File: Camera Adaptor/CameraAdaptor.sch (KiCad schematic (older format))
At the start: 6 parts

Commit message: Did the basic layout, avaiting via size, track width specifications.
Signed-off-by: Kolijn Wolfaardt <kolijn.wolfaardt@gmail.com>
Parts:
- C1: renamed from C?; footprint (none) -> Capacitors_SMD:C_1206_HandSoldering
- P1: renamed from P?; footprint (none) -> Pin_Headers:Pin_Header_Straight_2x12
- P2: renamed from P?; footprint (none) -> Pin_Headers:Pin_Header_Straight_2x09
- R1, R2: renamed from 4k7; value R -> 4.7k; footprint (none) -> Resistors_SMD:R_1206_HandSoldering
- U1: renamed from U?; footprint (none) -> oscillator:oscillator
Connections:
- no-connect marks 3 -> 4
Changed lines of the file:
@@
 $EndDescr
 $Comp
-L CONN_02X12 P?
+L CONN_02X12 P1
 U 1 1 5583E006
 P 3350 3250
-F 0 "P?" H 3350 3900 50  0000 C CNN
+F 0 "P1" H 3350 3900 50  0000 C CNN
 F 1 "CONN_02X12" V 3350 3250 50  0000 C CNN
-F 2 "" H 3350 2050 60  0000 C CNN
+F 2 "Pin_Headers:Pin_Header_Straight_2x12" H 3350 2050 60  0001 C CNN
 F 3 "" H 3350 2050 60  0000 C CNN
 	1    3350 3250
@@
 $EndComp
 $Comp
-L CONN_02X09 P?
+L CONN_02X09 P2
 U 1 1 5583E070
 P 5850 3200
-F 0 "P?" H 5850 3700 50  0000 C CNN
+F 0 "P2" H 5850 3700 50  0000 C CNN
 F 1 "CONN_02X09" V 5850 3200 50  0000 C CNN
-F 2 "" H 5850 2000 60  0000 C CNN
+F 2 "Pin_Headers:Pin_Header_Straight_2x09" H 5850 2000 60  0001 C CNN
 F 3 "" H 5850 2000 60  0000 C CNN
 	1    5850 3200
@@
 D0
 $Comp
-L R 4k7
+L R R1
 U 1 1 55C45043
 P 4550 1850
-F 0 "4k7" V 4630 1850 50  0000 C CNN
-F 1 "R" V 4550 1850 50  0000 C CNN
-F 2 "" V 4480 1850 30  0000 C CNN
+F 0 "R1" V 4630 1850 50  0000 C CNN
+F 1 "4.7k" V 4550 1850 50  0000 C CNN
+F 2 "Resistors_SMD:R_1206_HandSoldering" V 4480 1850 30  0001 C CNN
 F 3 "" H 4550 1850 30  0000 C CNN
 	1    4550 1850
@@
 $EndComp
 $Comp
-L R 4k7
+L R R2
 U 1 1 55C450E0
 P 4800 1850
-F 0 "4k7" V 4880 1850 50  0000 C CNN
-F 1 "R" V 4800 1850 50  0000 C CNN
-F 2 "" V 4730 1850 30  0000 C CNN
+F 0 "R2" V 4880 1850 50  0000 C CNN
+F 1 "4.7k" V 4800 1850 50  0000 C CNN
+F 2 "Resistors_SMD:R_1206_HandSoldering" V 4730 1850 30  0001 C CNN
 F 3 "" H 4800 1850 30  0000 C CNN
 	1    4800 1850
@@
 $EndComp
 $Comp
-L GND #PWR?
+L GND #PWR01
 U 1 1 55C45174
 P 4200 2700
-F 0 "#PWR?" H 4200 2450 50  0001 C CNN
+F 0 "#PWR01" H 4200 2450 50  0001 C CNN
 F 1 "GND" H 4200 2550 50  0000 C CNN
 F 2 "" H 4200 2700 60  0000 C CNN
@@
 $EndComp
 $Comp
-L +3.3V #PWR?
+L +3.3V #PWR02
 U 1 1 55C451A0
 P 2500 2700
-F 0 "#PWR?" H 2500 2550 50  0001 C CNN
+F 0 "#PWR02" H 2500 2550 50  0001 C CNN
 F 1 "+3.3V" H 2500 2840 50  0000 C CNN
 F 2 "" H 2500 2700 60  0000 C CNN
@@
 $EndComp
 $Comp
-L +3.3V #PWR?
+L +3.3V #PWR03
 U 1 1 55C45250
 P 4700 1600
-F 0 "#PWR?" H 4700 1450 50  0001 C CNN
+F 0 "#PWR03" H 4700 1450 50  0001 C CNN
 F 1 "+3.3V" H 4700 1740 50  0000 C CNN
 F 2 "" H 4700 1600 60  0000 C CNN
@@
 NoConn ~ 3600 3800
 $Comp
-L GND #PWR?
+L GND #PWR04
 U 1 1 55C45C7F
 P 4200 3450
-F 0 "#PWR?" H 4200 3200 50  0001 C CNN
+F 0 "#PWR04" H 4200 3200 50  0001 C CNN
 F 1 "GND" H 4200 3300 50  0000 C CNN
 F 2 "" H 4200 3450 60  0000 C CNN
@@
 	2500 3400 3100 3400
 $Comp
-L C C?
+L C C1
 U 1 1 55C45D20
 P 3100 1850
-F 0 "C?" H 3125 1950 50  0000 L CNN
+F 0 "C1" H 3125 1950 50  0000 L CNN
 F 1 "1uF" H 3125 1750 50  0000 L CNN
-F 2 "" H 3138 1700 30  0000 C CNN
+F 2 "Capacitors_SMD:C_1206_HandSoldering" H 3138 1700 30  0001 C CNN
 F 3 "" H 3100 1850 60  0000 C CNN
 	1    3100 1850
@@
 $EndComp
 $Comp
-L +3.3V #PWR?
+L +3.3V #PWR05
 U 1 1 55C45D93
 P 3100 1650
-F 0 "#PWR?" H 3100 1500 50  0001 C CNN
+F 0 "#PWR05" H 3100 1500 50  0001 C CNN
 F 1 "+3.3V" H 3100 1790 50  0000 C CNN
 F 2 "" H 3100 1650 60  0000 C CNN
@@
 $EndComp
 $Comp
-L GND #PWR?
+L GND #PWR06
 U 1 1 55C45DA8
 P 3100 2050
-F 0 "#PWR?" H 3100 1800 50  0001 C CNN
+F 0 "#PWR06" H 3100 1800 50  0001 C CNN
 F 1 "GND" H 3100 1900 50  0000 C CNN
 F 2 "" H 3100 2050 60  0000 C CNN
@@
 	3100 1700 3100 1650
 $Comp
-L Oscillator U?
+L Oscillator U1
 U 1 1 55C47029
 P 4500 4650
-F 0 "U?" H 4500 4400 60  0000 C CNN
+F 0 "U1" H 4500 4400 60  0000 C CNN
 F 1 "Oscillator" H 4500 4900 60  0000 C CNN
-F 2 "" H 4500 4650 60  0000 C CNN
+F 2 "oscillator:oscillator" H 4500 4650 60  0001 C CNN
 F 3 "" H 4500 4650 60  0000 C CNN
 	1    4500 4650
@@
 $EndComp
 $Comp
-L +3.3V #PWR?
+L +3.3V #PWR07
 U 1 1 55C47102
 P 5100 4450
-F 0 "#PWR?" H 5100 4300 50  0001 C CNN
+F 0 "#PWR07" H 5100 4300 50  0001 C CNN
 F 1 "+3.3V" H 5100 4590 50  0000 C CNN
 F 2 "" H 5100 4450 60  0000 C CNN
@@
 	5100 4550 5100 4450
 $Comp
-L GND #PWR?
+L GND #PWR08
 U 1 1 55C471E4
 P 3900 4850
-F 0 "#PWR?" H 3900 4600 50  0001 C CNN
+F 0 "#PWR08" H 3900 4600 50  0001 C CNN
 F 1 "GND" H 3900 4700 50  0000 C CNN
 F 2 "" H 3900 4850 60  0000 C CNN
@@
 PCLK
 $Comp
-L +3.3V #PWR?
+L +3.3V #PWR09
 U 1 1 55C476CA
 P 3900 4450
-F 0 "#PWR?" H 3900 4300 50  0001 C CNN
+F 0 "#PWR09" H 3900 4300 50  0001 C CNN
 F 1 "+3.3V" H 3900 4590 50  0000 C CNN
 F 2 "" H 3900 4450 60  0000 C CNN
@@
 Wire Wire Line
 	3900 4550 4000 4550
+NoConn ~ 3100 3600
 $EndSCHEMATC

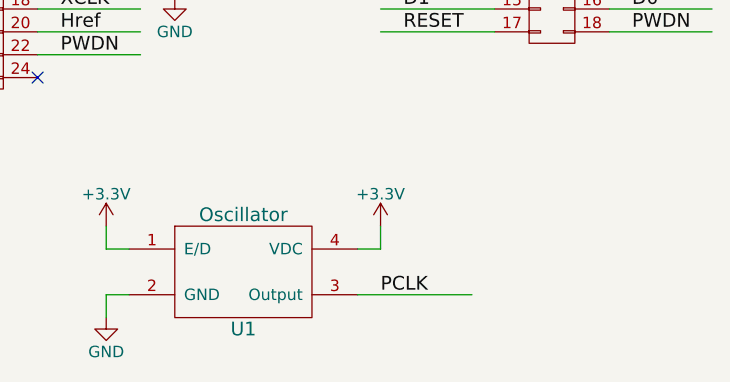
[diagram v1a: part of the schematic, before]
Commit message: Changed CamerAdaptor layout, changed track thickness
Signed-off-by: Kolijn Wolfaardt <kolijn.wolfaardt@gmail.com>
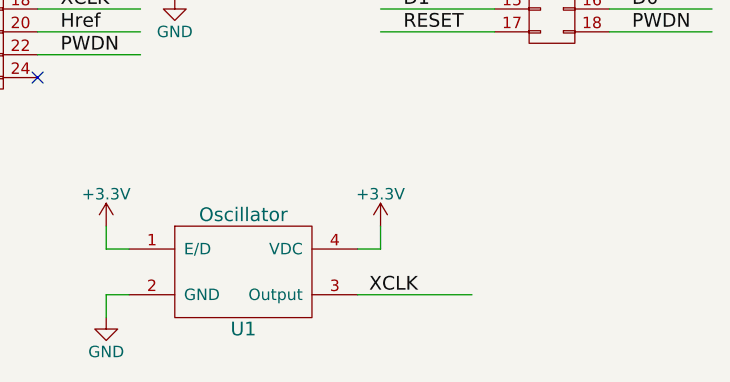
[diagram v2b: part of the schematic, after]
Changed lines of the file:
@@
 Wire Wire Line
 	5500 4750 5000 4750
-Text Label 5100 4750 0    60   ~ 0
-PCLK
 $Comp
 L +3.3V #PWR09
@@
 	3900 4550 4000 4550
 NoConn ~ 3100 3600
+Text Label 5050 4750 0    60   ~ 0
+XCLK
 $EndSCHEMATC
